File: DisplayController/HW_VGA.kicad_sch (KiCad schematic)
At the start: 7 parts, among them J1 Conn_02x40_Odd_Even, J301 Conn_01x02, J401 Conn_01x06, U1 25.175 MHz, U301 GAL22V10

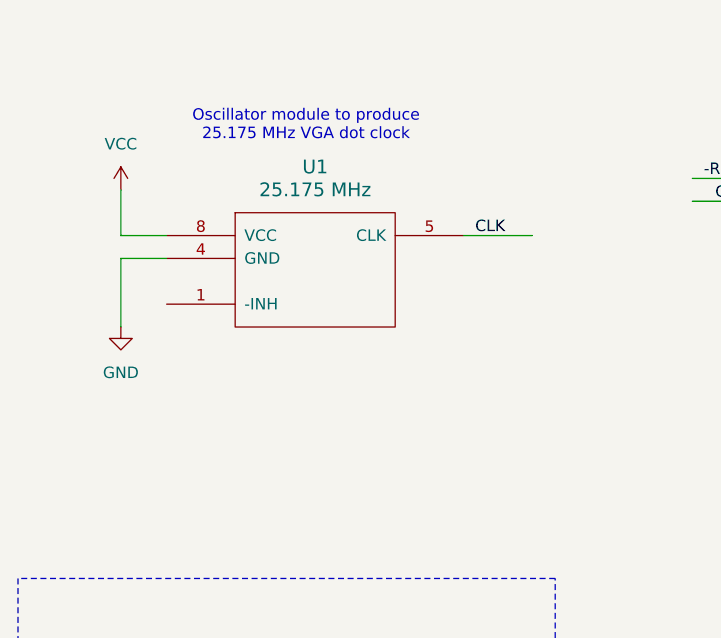
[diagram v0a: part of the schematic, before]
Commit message: starting footprint assignment
Changed oscillator module to KiCad-provided 7050.
(Need to check whether the footprint will work with the
SG636P oscillators I'm using. (I think it will, but I
need to measure.)
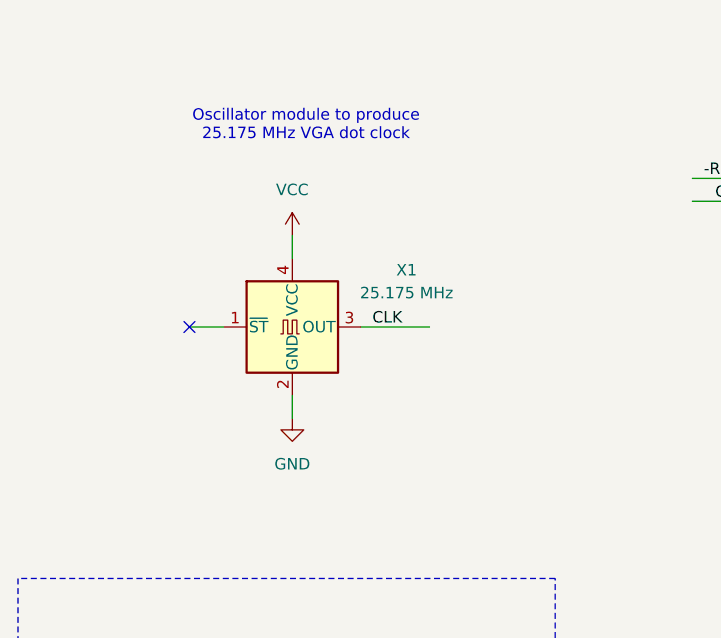
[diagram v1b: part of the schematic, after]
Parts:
- removed U1: 25.175 MHz, symbol ya68k:XTAL_OSC_HALF_CAN
- added X1: 25.175 MHz, Oscillator:Oscillator_SMD_SeikoEpson_SG8002CA-4Pin_7.0x5.0mm, symbol Oscillator:SG-7050CAN
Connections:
- net CLK: now also X1.3 (OUT)
- net GND: now also X1.2 (GND)
- net VCC: now also X1.4 (VCC)
- no-connect marks 0 -> 1
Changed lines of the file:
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@@
 		(company "daveho hacks")
 	)
+	(no_connect
+		(at 36.83 53.34)
+	)
 	(wire
 		(pts
@@
 	(wire
 		(pts
-			(xy 29.21 45.72) (xy 29.21 53.34)
-		)
-		(stroke
-			(width 0)
-			(type default)
-		)
-	)
-	(wire
-		(pts
 			(xy 83.82 166.37) (xy 104.14 166.37)
 		)
@@
 	(wire
 		(pts
+			(xy 48.26 60.96) (xy 48.26 63.5)
+		)
+		(stroke
+			(width 0)
+			(type default)
+		)
+	)
+	(wire
+		(pts
 			(xy 143.51 125.73) (xy 161.29 125.73)
 		)
@@
 	(wire
 		(pts
-			(xy 34.29 45.72) (xy 29.21 45.72)
-		)
-		(stroke
-			(width 0)
-			(type default)
-		)
-	)
-	(wire
-		(pts
 			(xy 175.26 143.51) (xy 190.5 143.51)
 		)
@@
 	(wire
 		(pts
-			(xy 67.31 43.18) (xy 74.93 43.18)
+			(xy 55.88 53.34) (xy 63.5 53.34)
 		)
 		(stroke
@@
 	(wire
 		(pts
-			(xy 34.29 43.18) (xy 29.21 43.18)
-		)
-		(stroke
-			(width 0)
-			(type default)
-		)
-	)
-	(wire
-		(pts
 			(xy 125.73 67.31) (xy 142.24 67.31)
 		)
@@
 	(wire
 		(pts
-			(xy 29.21 38.1) (xy 29.21 43.18)
-		)
-		(stroke
-			(width 0)
-			(type default)
-		)
-	)
-	(wire
-		(pts
 			(xy 302.26 127) (xy 320.04 127)
 		)
@@
 	(wire
 		(pts
+			(xy 36.83 53.34) (xy 40.64 53.34)
+		)
+		(stroke
+			(width 0)
+			(type default)
+		)
+	)
+	(wire
+		(pts
 			(xy 243.84 44.45) (xy 241.3 44.45)
 		)
@@
 	(wire
 		(pts
+			(xy 48.26 43.18) (xy 48.26 45.72)
+		)
+		(stroke
+			(width 0)
+			(type default)
+		)
+	)
+	(wire
+		(pts
 			(xy 175.26 138.43) (xy 190.5 138.43)
 		)
@@
 	)
 	(label "CLK"
-		(at 68.58 43.18 0)
+		(at 57.15 53.34 0)
 		(fields_autoplaced yes)
 		(effects
@@
 	(symbol
 		(lib_id "power:GND")
-		(at 29.21 53.34 0)
+		(at 48.26 63.5 0)
 		(unit 1)
 		(exclude_from_sim no)
@@
 		(fields_autoplaced yes)
 		(property "Reference" "#PWR02"
-			(at 29.21 59.69 0)
+			(at 48.26 69.85 0)
 			(effects
 				(font
@@
 		)
 		(property "Value" "GND"
-			(at 29.21 58.42 0)
+			(at 48.26 68.58 0)
 			(effects
 				(font
@@
 		)
 		(property "Footprint" ""
-			(at 29.21 53.34 0)
+			(at 48.26 63.5 0)
 			(effects
 				(font
@@
 		)
 		(property "Datasheet" ""
-			(at 29.21 53.34 0)
+			(at 48.26 63.5 0)
 			(effects
 				(font
@@
 		)
 		(property "Description" ""
-			(at 29.21 53.34 0)
+			(at 48.26 63.5 0)
 			(effects
 				(font
@@
 	)
 	(symbol
-		(lib_id "ya68k:XTAL_OSC_HALF_CAN")
-		(at 50.8 46.99 0)
-		(unit 1)
-		(exclude_from_sim no)
-		(in_bom yes)
-		(on_board yes)
-		(dnp no)
-		(fields_autoplaced yes)
-		(property "Reference" "U1"
-			(at 50.8 35.56 0)
-			(effects
-				(font
-					(size 1.524 1.524)
-				)
-			)
-		)
-		(property "Value" "25.175 MHz"
-			(at 50.8 38.1 0)
-			(effects
-				(font
-					(size 1.524 1.524)
-				)
-			)
-		)
-		(property "Footprint" ""
-			(at 50.8 46.99 0)
-			(effects
-				(font
-					(size 1.524 1.524)
-				)
-			)
-		)
-		(property "Datasheet" ""
-			(at 50.8 46.99 0)
-			(effects
-				(font
-					(size 1.524 1.524)
-				)
-			)
-		)
-		(property "Description" ""
-			(at 50.8 46.99 0)
-			(effects
-				(font
-					(size 1.27 1.27)
-				)
-				(hide yes)
-			)
-		)
-		(pin "5"
-		)
-		(pin "1"
-		)
-		(pin "4"
-		)
-		(pin "8"
-		)
-		(instances
-			(project "HW_VGA"
-				(path "/c4bd4b39-993a-4195-805f-b4de6fa4aea5"
-					(reference "U1")
-					(unit 1)
-				)
-			)
-		)
-	)
-	(symbol
 		(lib_id "Device:C")
 		(at 289.56 31.75 0)
@@
 	(symbol
 		(lib_id "power:VCC")
-		(at 29.21 38.1 0)
+		(at 48.26 43.18 0)
 		(unit 1)
 		(exclude_from_sim no)
@@
 		(fields_autoplaced yes)
 		(property "Reference" "#PWR01"
-			(at 29.21 41.91 0)
+			(at 48.26 46.99 0)
 			(effects
 				(font
@@
 		)
 		(property "Value" "VCC"
-			(at 29.21 33.02 0)
+			(at 48.26 38.1 0)
 			(effects
 				(font
@@
 		)
 		(property "Footprint" ""
-			(at 29.21 38.1 0)
+			(at 48.26 43.18 0)
 			(effects
 				(font
@@
 		)
 		(property "Datasheet" ""
-			(at 29.21 38.1 0)
+			(at 48.26 43.18 0)
 			(effects
 				(font
@@
 		)
 		(property "Description" ""
-			(at 29.21 38.1 0)
+			(at 48.26 43.18 0)
 			(effects
 				(font
@@
 	)
 	(symbol
+		(lib_id "Oscillator:SG-7050CAN")
+		(at 48.26 53.34 0)
+		(unit 1)
+		(exclude_from_sim no)
+		(in_bom yes)
+		(on_board yes)
+		(dnp no)
+		(fields_autoplaced yes)
+		(property "Reference" "X1"
+			(at 60.96 47.0214 0)
+			(effects
+				(font
+					(size 1.27 1.27)
+				)
+			)
+		)
+		(property "Value" "25.175 MHz"
+			(at 60.96 49.5614 0)
+			(effects
+				(font
+					(size 1.27 1.27)
+				)
+			)
+		)
+		(property "Footprint" "Oscillator:Oscillator_SMD_SeikoEpson_SG8002CA-4Pin_7.0x5.0mm"
+			(at 66.04 62.23 0)
+			(effects
+				(font
+					(size 1.27 1.27)
+				)
+				(hide yes)
+			)
+		)
+		(property "Datasheet" "https://support.epson.biz/td/api/doc_check.php?dl=brief_SG7050CAN&lang=en"
+			(at 45.72 53.34 0)
+			(effects
+				(font
+					(size 1.27 1.27)
+				)
+				(hide yes)
+			)
+		)
+		(property "Description" "CMOS Clock Oscillator 1 to 75 MHz"
+			(at 48.26 53.34 0)
+			(effects
+				(font
+					(size 1.27 1.27)
+				)
+				(hide yes)
+			)
+		)
+		(pin "3"
+		)
+		(pin "1"
+		)
+		(pin "4"
+		)
+		(pin "2"
+		)
+		(instances
+			(project ""
+				(path "/c4bd4b39-993a-4195-805f-b4de6fa4aea5"
+					(reference "X1")
+					(unit 1)
+				)
+			)
+		)
+	)
+	(symbol
 		(lib_id "device:CP")
 		(at 36.83 226.06 0)
@@
 					(size 1.524 1.524)
 				)
+				(hide yes)
 			)
 		)

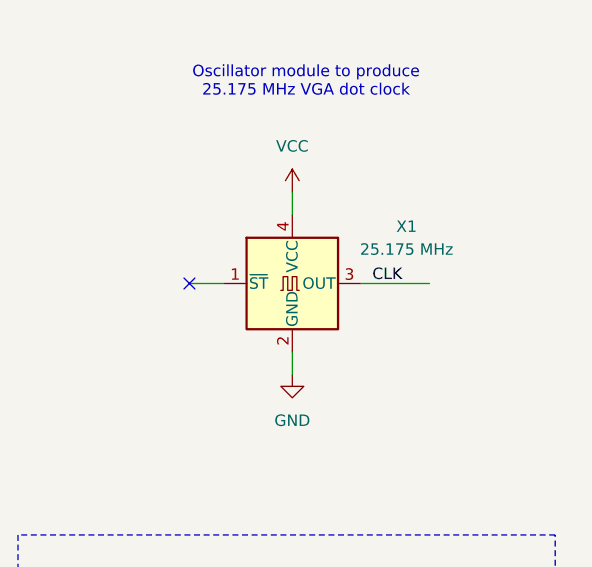
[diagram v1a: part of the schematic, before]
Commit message: add bypass cap for oscillator module
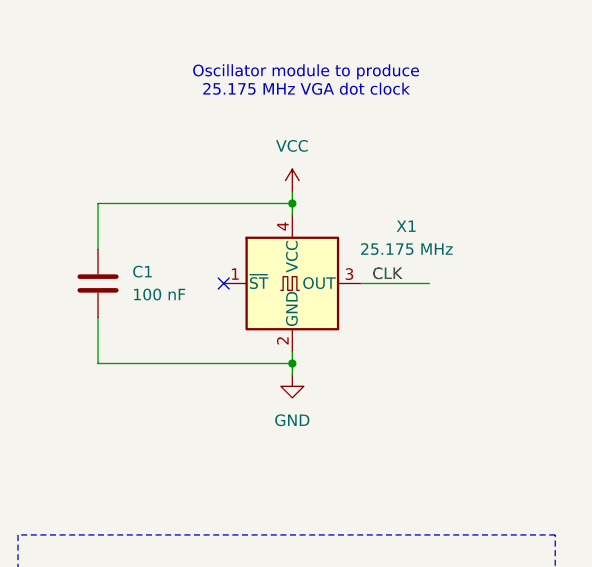
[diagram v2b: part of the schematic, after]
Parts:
- added C1: 100 nF, symbol Device:C
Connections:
- net GND: now also C1.2
- net VCC: now also C1.1
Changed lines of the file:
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@@
 		(company "daveho hacks")
 	)
+	(junction
+		(at 48.26 62.23)
+		(diameter 0)
+		(color 0 0 0 0)
+	)
+	(junction
+		(at 48.26 44.45)
+		(diameter 0)
+		(color 0 0 0 0)
+	)
 	(no_connect
-		(at 36.83 53.34)
+		(at 40.64 53.34)
 	)
 	(wire
@@
 	(wire
 		(pts
+			(xy 26.67 62.23) (xy 48.26 62.23)
+		)
+		(stroke
+			(width 0)
+			(type default)
+		)
+	)
+	(wire
+		(pts
 			(xy 252.73 195.58) (xy 267.97 195.58)
 		)
@@
 	(wire
 		(pts
-			(xy 48.26 60.96) (xy 48.26 63.5)
+			(xy 48.26 60.96) (xy 48.26 62.23)
 		)
 		(stroke
@@
 	(wire
 		(pts
+			(xy 26.67 44.45) (xy 48.26 44.45)
+		)
+		(stroke
+			(width 0)
+			(type default)
+		)
+	)
+	(wire
+		(pts
 			(xy 252.73 198.12) (xy 267.97 198.12)
 		)
@@
 	(wire
 		(pts
+			(xy 48.26 44.45) (xy 48.26 45.72)
+		)
+		(stroke
+			(width 0)
+			(type default)
+		)
+	)
+	(wire
+		(pts
 			(xy 229.87 52.07) (xy 243.84 52.07)
 		)
@@
 	(wire
 		(pts
+			(xy 48.26 62.23) (xy 48.26 63.5)
+		)
+		(stroke
+			(width 0)
+			(type default)
+		)
+	)
+	(wire
+		(pts
 			(xy 53.34 194.31) (xy 67.31 194.31)
 		)
@@
 	(wire
 		(pts
-			(xy 36.83 53.34) (xy 40.64 53.34)
-		)
-		(stroke
-			(width 0)
-			(type default)
-		)
-	)
-	(wire
-		(pts
 			(xy 243.84 44.45) (xy 241.3 44.45)
 		)
@@
 	(wire
 		(pts
+			(xy 26.67 49.53) (xy 26.67 44.45)
+		)
+		(stroke
+			(width 0)
+			(type default)
+		)
+	)
+	(wire
+		(pts
 			(xy 53.34 189.23) (xy 67.31 189.23)
 		)
@@
 	(wire
 		(pts
+			(xy 26.67 57.15) (xy 26.67 62.23)
+		)
+		(stroke
+			(width 0)
+			(type default)
+		)
+	)
+	(wire
+		(pts
 			(xy 83.82 138.43) (xy 104.14 138.43)
 		)
@@
 	(wire
 		(pts
-			(xy 48.26 43.18) (xy 48.26 45.72)
+			(xy 48.26 43.18) (xy 48.26 44.45)
 		)
 		(stroke
@@
 					(unit 1)
 				)
+			)
+		)
+	)
+	(symbol
+		(lib_id "Device:C")
+		(at 26.67 53.34 0)
+		(unit 1)
+		(exclude_from_sim no)
+		(in_bom yes)
+		(on_board yes)
+		(dnp no)
+		(fields_autoplaced yes)
+		(property "Reference" "C1"
+			(at 30.48 52.0699 0)
+			(effects
+				(font
+					(size 1.27 1.27)
+				)
+				(justify left)
+			)
+		)
+		(property "Value" "100 nF"
+			(at 30.48 54.6099 0)
+			(effects
+				(font
+					(size 1.27 1.27)
+				)
+				(justify left)
+			)
+		)
+		(property "Footprint" ""
+			(at 27.6352 57.15 0)
+			(effects
+				(font
+					(size 1.27 1.27)
+				)
+				(hide yes)
+			)
+		)
+		(property "Datasheet" "~"
+			(at 26.67 53.34 0)
+			(effects
+				(font
+					(size 1.27 1.27)
+				)
+				(hide yes)
+			)
+		)
+		(property "Description" "Unpolarized capacitor"
+			(at 26.67 53.34 0)
+			(effects
+				(font
+					(size 1.27 1.27)
+				)
+				(hide yes)
+			)
+		)
+		(pin "2"
+		)
+		(pin "1"
+		)
+		(instances
+			(project ""
+				(path "/c4bd4b39-993a-4195-805f-b4de6fa4aea5"
+					(reference "C1")
+					(unit 1)
+				)

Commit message: assigned footprints
Will need to double check.
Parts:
- C1, C301: footprint (none) -> Capacitor_SMD:C_0805_2012Metric_Pad1.18x1.45mm_HandSolder
- J301: footprint (none) -> Connector_PinHeader_2.54mm:PinHeader_1x01_P2.54mm_Vertical
- J401: footprint (none) -> Connector_PinHeader_2.54mm:PinHeader_1x06_P2.54mm_Vertical
- U301: footprint (none) -> Package_DIP:DIP-24_W7.62mm_Socket
- X1: footprint Oscillator:Oscillator_SMD_SeikoEpson_SG8002CA-4Pin_7.0x5.0mm -> SG-636P:SG-636P
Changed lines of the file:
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@@
 			)
 		)
-		(property "Footprint" ""
+		(property "Footprint" "Capacitor_SMD:C_0805_2012Metric_Pad1.18x1.45mm_HandSolder"
 			(at 27.6352 57.15 0)
 			(effects
@@
 			)
 		)
-		(property "Footprint" ""
+		(property "Footprint" "Capacitor_SMD:C_0805_2012Metric_Pad1.18x1.45mm_HandSolder"
 			(at 290.5252 35.56 0)
 			(effects
@@
 			)
 		)
-		(property "Footprint" ""
+		(property "Footprint" "Connector_PinHeader_2.54mm:PinHeader_1x01_P2.54mm_Vertical"
 			(at 303.53 54.61 0)
 			(effects
@@
 			)
 		)
-		(property "Footprint" ""
+		(property "Footprint" "Connector_PinHeader_2.54mm:PinHeader_1x06_P2.54mm_Vertical"
 			(at 306.07 170.18 0)
 			(effects
@@
 			)
 		)
-		(property "Footprint" "Oscillator:Oscillator_SMD_SeikoEpson_SG8002CA-4Pin_7.0x5.0mm"
+		(property "Footprint" "SG-636P:SG-636P"
 			(at 66.04 62.23 0)
 			(effects
@@
 			)
 		)
-		(property "Footprint" ""
+		(property "Footprint" "Package_DIP:DIP-24_W7.62mm_Socket"
 			(at 261.62 60.96 0)
 			(effects

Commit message: fixed an incorrect footprint assignment
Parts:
- J301: footprint Connector_PinHeader_2.54mm:PinHeader_1x01_P2.54mm_Vertical -> Connector_PinHeader_2.54mm:PinHeader_1x02_P2.54mm_Vertical
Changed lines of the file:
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@@
 			)
 		)
-		(property "Footprint" "Connector_PinHeader_2.54mm:PinHeader_1x01_P2.54mm_Vertical"
+		(property "Footprint" "Connector_PinHeader_2.54mm:PinHeader_1x02_P2.54mm_Vertical"
 			(at 303.53 54.61 0)
 			(effects

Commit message: fixed wiring of VGA output connector
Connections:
- net Output/Bout: now also J401.3 (Pin_3); no longer J401.1 (Pin_1)
- net Output/Rout: now also J401.1 (Pin_1); no longer J401.3 (Pin_3)
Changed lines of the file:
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@@
 		)
 		(pin "Bout" output
-			(at 289.56 165.1 0)
+			(at 289.56 170.18 0)
 			(effects
 				(font
@@
 		)
 		(pin "Rout" output
-			(at 289.56 170.18 0)
+			(at 289.56 165.1 0)
 			(effects
 				(font

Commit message: initial PCB component placement
Changed package for GAL22V10 to SOIC24 rather than DIP24.
That means we'll use ATF22V10C parts (which are available
as SOIC24.)

Now for the routing :-)
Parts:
- U301: footprint Package_DIP:DIP-24_W7.62mm_Socket -> Package_SO:SOIC-24W_7.5x15.4mm_P1.27mm
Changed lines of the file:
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@@
 			)
 		)
-		(property "Footprint" "Package_DIP:DIP-24_W7.62mm_Socket"
+		(property "Footprint" "Package_SO:SOIC-24W_7.5x15.4mm_P1.27mm"
 			(at 261.62 60.96 0)
 			(effects

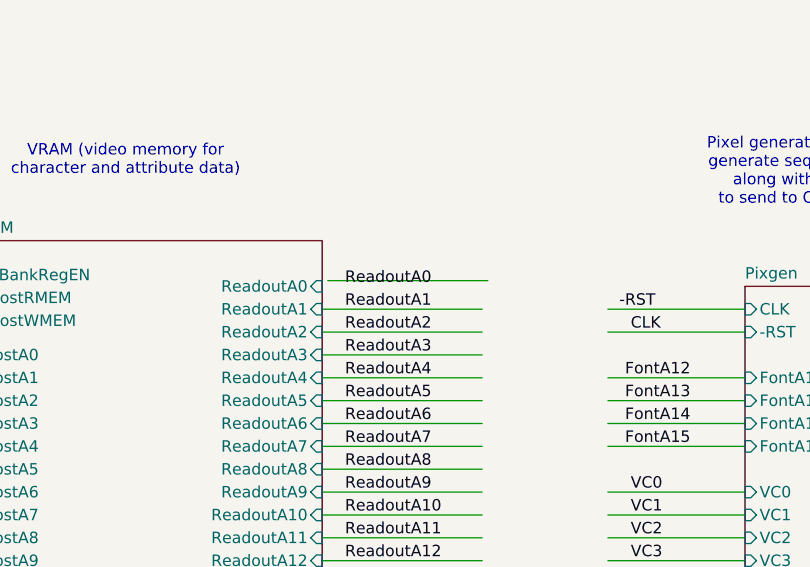
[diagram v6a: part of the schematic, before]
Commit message: bugfix: ReadoutA0 wasn't connected
A wire was misplaced on the main sheet, which meant
that the ReadoutA0 input of the VRAM module had no
connection to the ReadoutA0 output from the Readout
module.

This will require a bodge wire on the 29-Jul-2024
version of the PCB, but fortunately it will be a very
easy one, since the 74ALS163 that generates ReadoutA0
is on the bottom of the PCB and can be easily connected
to the appropriate pin on either VRAM PLCC socket.
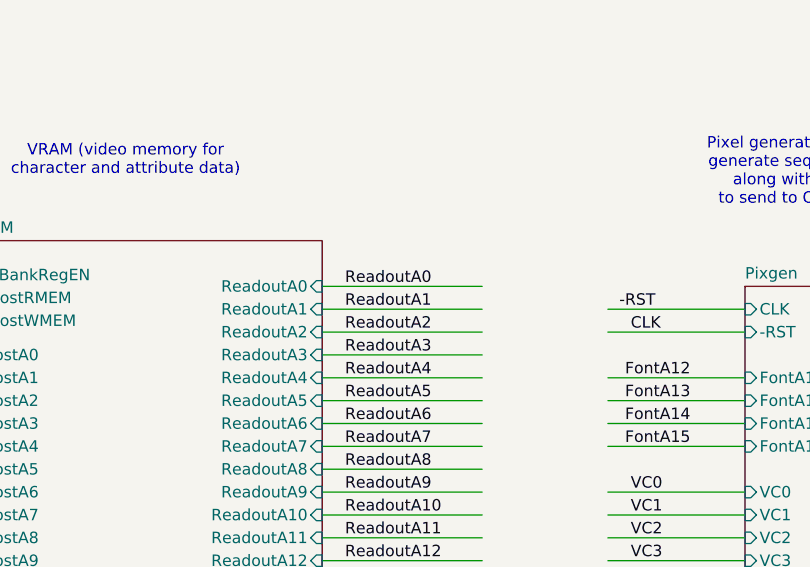
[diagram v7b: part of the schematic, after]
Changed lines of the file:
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@@
 	(wire
 		(pts
-			(xy 144.145 120.015) (xy 161.925 120.015)
+			(xy 143.51 120.65) (xy 161.29 120.65)
 		)
 		(stroke
